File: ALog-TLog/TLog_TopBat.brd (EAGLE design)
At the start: 124.1 x 45.3 mm, 101 parts, among them IC1 ATMEGA644M, J6 5.5x2.1mm Barrel, Q5 MOSFET_PCH-IRLML2244, Q6 MOSFET_PCH-IRLML2244, Q7 MOSFET_PCH-IRLML2244, Q8 MOSFET-NCH-BSS138, Q9 MOSFET-NCH-BSS138, U2 FT231X-Q, U3 915MHz, U4 SX1509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

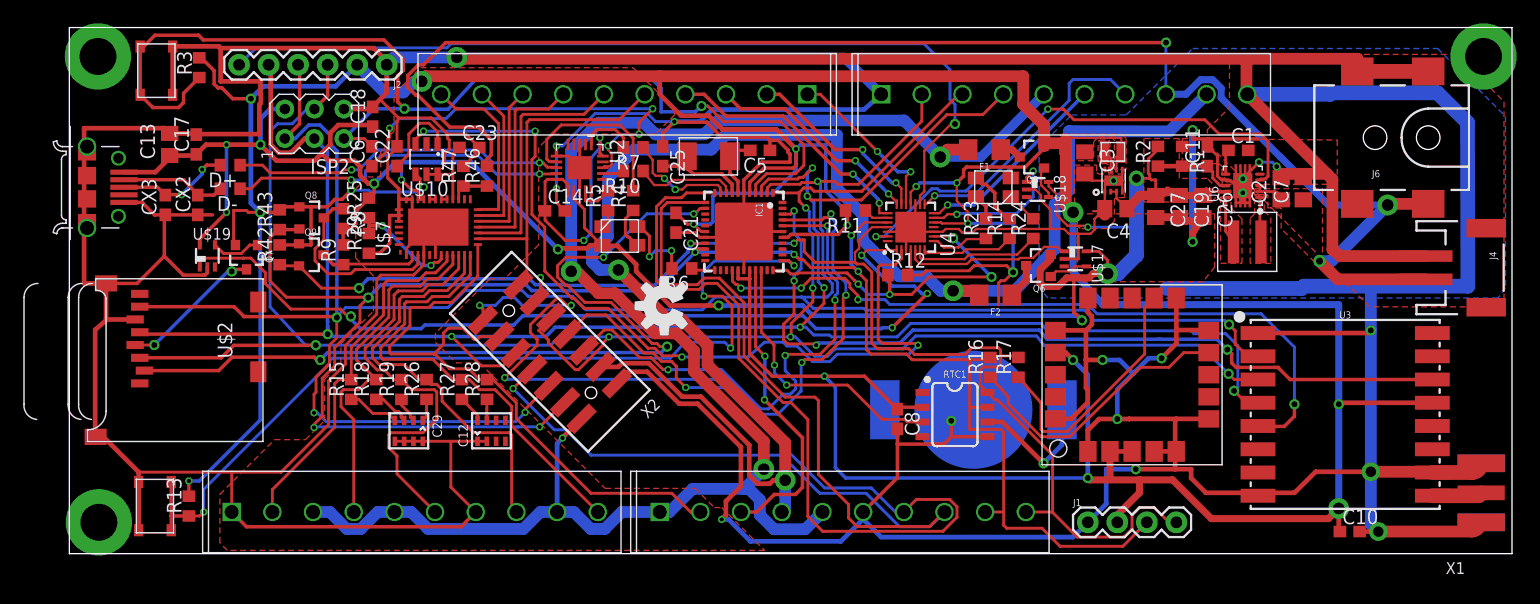
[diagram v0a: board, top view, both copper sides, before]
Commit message: Added AliveLED connection, cleaned up board, made gerbers
Connected the green channel of the TX RX RGB LED to be a "built in" LED for the board, in order to indicate lowest level of functionality, so as to not need the IO expander. Also did some basic clean up of the board and generated preliminary gerber files (current gerbers do not have fancy silk screen in them to speed up generation and analysis time)
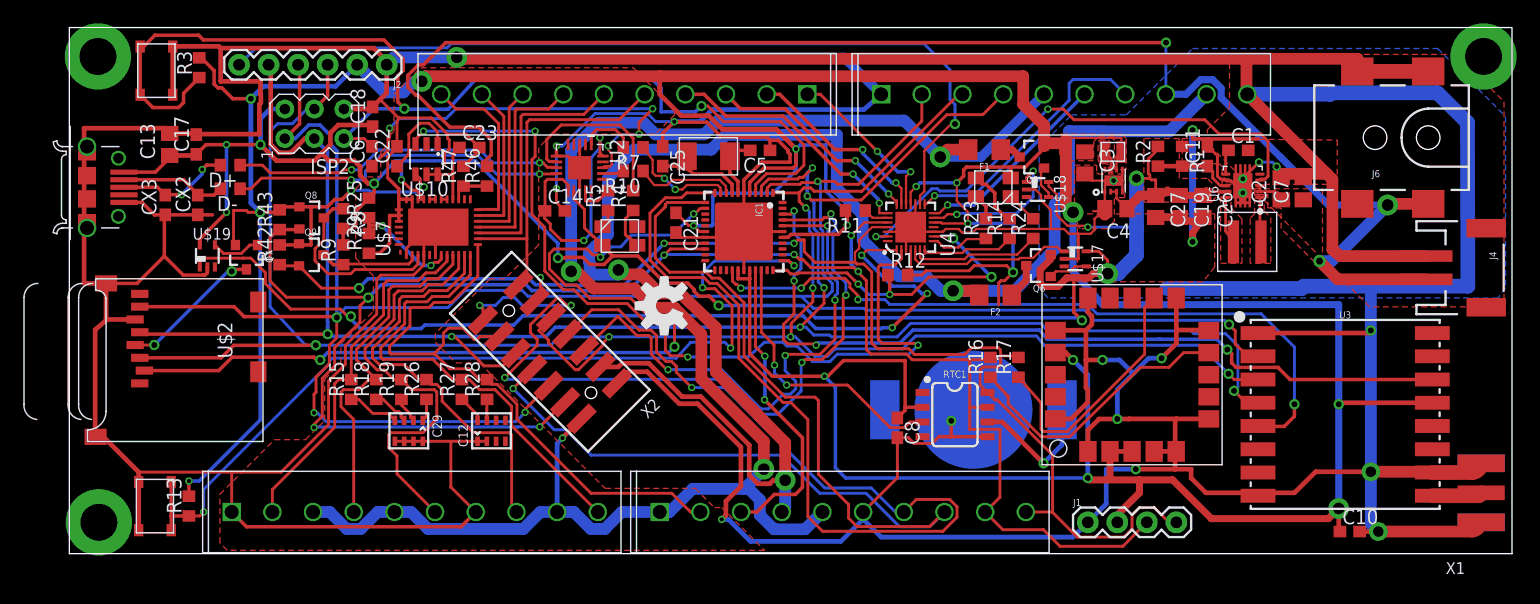
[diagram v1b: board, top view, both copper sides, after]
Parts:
- removed R6: 330, bschulz_passives:R0603
- moved C8 0.76 mm to (71.4, 10.9)
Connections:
- removed net ALIVE_LED: R6.2, U$16.4
- removed net N$33: IC1.23, R6.1
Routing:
- net ALIVE_LED: track 6.80 -> 0.00 mm, vias 2 -> 0
- net SD_CS: track 73.7 -> 78.4 mm
- net 3V3: track 426.5 -> 431.2 mm
- net EXT_5V: track 137.4 -> 140.1 mm
- net SDA: track 156.3 -> 158.7 mm
- net 5V: track 185.7 -> 187.9 mm
- net SCL: track 118.9 -> 121.0 mm
- net N$33: track 2.05 -> 0.00 mm
- net D1_UNIV: track 44.7 -> 46.6 mm
- net REF_CTRL: track 73.4 -> 74.8 mm
- net EXT_3.3V: track 147.6 -> 148.8 mm
- net MISO: track 192.2 -> 191.3 mm
- net TX_EXT: track 96.2 -> 95.4 mm
- net GND: track 841.3 -> 840.8 mm
